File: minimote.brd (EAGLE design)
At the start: 160 x 100 mm, 41 parts, among them IC1 ATTINY441/841-SSU, J1 AVR_SPI_PROG_3X2PTH, T1 2N3904

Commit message: moved parts around
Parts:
- removed U$3: EDGEUSB, minimote:USBPCB
- added U$13: EDGEUSB, minimote:USBPCB
- moved R10 141.0 mm to (3.81, 38.1), turned to 270 degrees
- moved R9 137.4 mm to (7.62, 38.1), turned to 270 degrees
- moved R8 134.9 mm to (11.4, 38.1), turned to 90 degrees
- moved C1 132.1 mm to (7.62, 29.2), turned to 90 degrees
- moved U$2 130.3 mm to (15.2, 38.1)
- moved C2 129.6 mm to (10.2, 29.2), turned to 90 degrees
- moved U$1 127.3 mm to (20.3, 38.1)
- moved R12 123.4 mm to (3.81, 30.5)
- moved R11 122.6 mm to (3.81, 27.9)
- moved R13 122.5 mm to (3.81, 19.1), turned to 270 degrees
- moved RN1 108.1 mm to (43.2, 63.5), turned to 90 degrees
- moved R1 100.1 mm to (17.8, 19.1), turned to 270 degrees
- moved R6 86.4 mm to (14.0, 19.1), turned to 270 degrees
- moved D2 83.7 mm to (25.4, 38.1)
- moved R4 83.0 mm to (25.4, 19.1), turned to 270 degrees
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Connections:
- new net N$123: D4.C, D5.A, D6.A, R1.2
- new net N$124: D1.C, D3.A, D4.A, D5.C, R4.2
- new net N$125: D1.A, D3.C, D6.C, R7.2
- net GND: now also U$13.GND; no longer U$3.GND
- net LED1: no longer D1.A, D3.C, D6.C, R7.2
- net LED2: no longer D1.C, D3.A, D4.A, D5.C, R4.2
- net LED3: no longer D4.C, D5.A, D6.A, R1.2
- net N$8: now also U$13.DM; no longer U$3.DM
- net N$9: now also U$13.DP; no longer U$3.DP
- net V_USB: now also U$13.VCC; no longer U$3.VCC
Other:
- board size 160 x 100 mm -> 85.6 x 54.2 mm

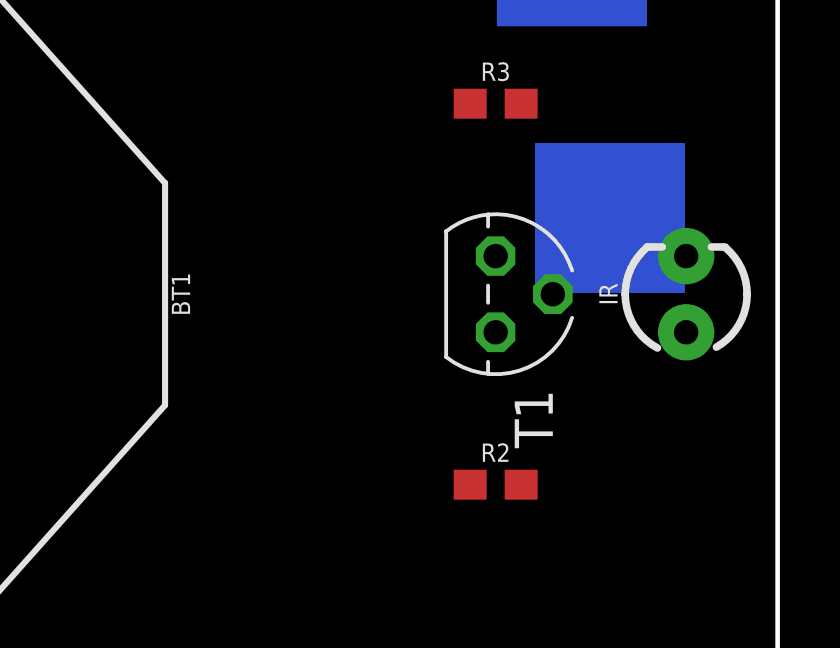
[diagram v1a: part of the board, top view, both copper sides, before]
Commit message: changed 3904 to smt component
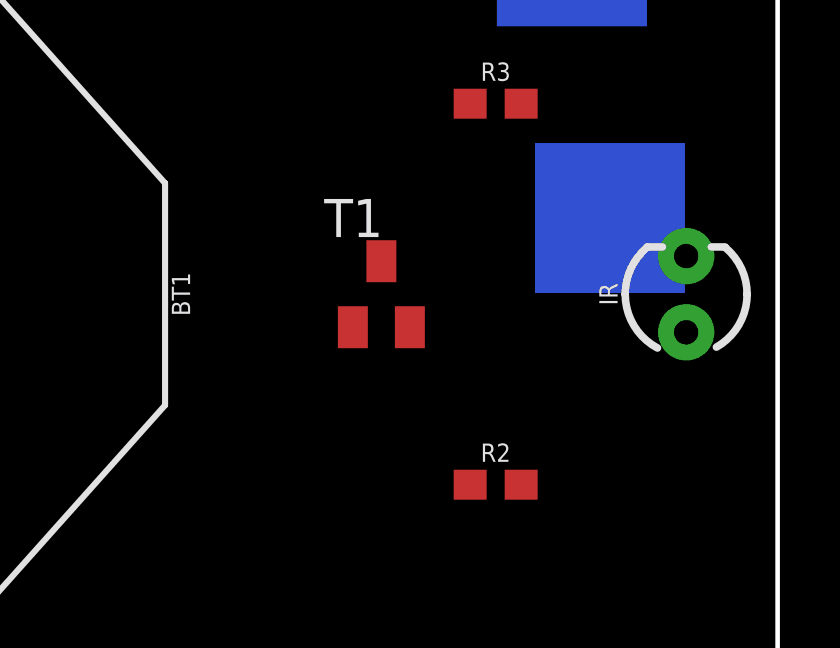
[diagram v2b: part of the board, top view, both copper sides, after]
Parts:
- T1: value 2N3904 -> (none); device transistor:TO92 -> transistor:SOT23-BEC
- moved T1 3.81 mm to (72.4, 27.9), turned to 0 degrees
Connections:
- net GND: now also T1.E; no longer T1.3
- net N$2: now also T1.C; no longer T1.1
- net N$3: now also T1.B; no longer T1.2
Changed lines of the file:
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@@
 <attribute name="SF_SKU" value="COM-08720" x="69.85" y="41.91" size="1.778" layer="27" rot="R90" display="off"/>
 </element>
-<element name="T1" library="transistor" library_urn="urn:adsk.eagle:library:402" package="TO92" package3d_urn="urn:adsk.eagle:package:29893/2" value="2N3904" x="76.2" y="27.94" rot="R270"/>
 <element name="U$1" library="minimote" package="SOT23" value="SI2301" x="20.32" y="38.1"/>
 <element name="R8" library="SparkFun-Resistors" library_urn="urn:adsk.eagle:library:532" package="0603" package3d_urn="urn:adsk.eagle:package:39650/1" value="10k" x="11.43" y="38.1" rot="R90">
@@
 <element name="U$13" library="minimote" package="USBPCB" value="EDGEUSB" x="0" y="22.86" rot="R90"/>
 <element name="U$4" library="minimote" package="SOT23" value="AZ23C3V6" x="8.89" y="19.05" rot="R180"/>
+<element name="T1" library="transistor" library_urn="urn:adsk.eagle:library:402" package="SOT23-BEC" package3d_urn="urn:adsk.eagle:package:29919/2" value="" x="72.39" y="27.94"/>
 </elements>
 <signals>
@@
 <contactref element="BT1" pad="2"/>
 <contactref element="J1" pad="6"/>
-<contactref element="T1" pad="3"/>
 <contactref element="S2" pad="3"/>
 <contactref element="S2" pad="4"/>
@@
 <contactref element="U$13" pad="GND"/>
 <contactref element="U$4" pad="3"/>
-<wire x1="71.755" y1="44.704" x2="76.2" y2="29.21" width="0" layer="19" extent="1-1"/>
+<contactref element="T1" pad="E"/>
 <wire x1="71.755" y1="39.116" x2="71.755" y2="44.704" width="0" layer="19" extent="1-1"/>
-<wire x1="54.61" y1="27.94" x2="71.755" y2="44.704" width="0" layer="19" extent="1-1"/>
+<wire x1="54.61" y1="27.94" x2="71.755" y2="39.116" width="0" layer="19" extent="1-1"/>
 <wire x1="35.56" y1="26.67" x2="54.61" y2="27.94" width="0" layer="19" extent="1-1"/>
-<wire x1="10.16" y1="30.06" x2="35.56" y2="26.67" width="0" layer="19" extent="1-1"/>
+<wire x1="16.19" y1="37" x2="35.56" y2="26.67" width="0" layer="19" extent="1-1"/>
+<wire x1="13.97" y1="32.21" x2="16.19" y2="37" width="0" layer="19" extent="1-1"/>
+<wire x1="10.16" y1="30.06" x2="13.97" y2="32.21" width="0" layer="19" extent="1-1"/>
 <wire x1="7.62" y1="30.06" x2="10.16" y2="30.06" width="0" layer="19" extent="1-1"/>
-<wire x1="16.19" y1="37" x2="7.62" y2="30.06" width="0" layer="19" extent="1-1"/>
-<wire x1="13.97" y1="32.21" x2="16.19" y2="37" width="0" layer="19" extent="1-1"/>
-<wire x1="-6.35" y1="32.7025" x2="13.97" y2="32.21" width="0" layer="19" extent="1-1"/>
-<wire x1="8.89" y1="17.95" x2="-6.35" y2="32.7025" width="0" layer="19" extent="1-1"/>
+<wire x1="8.89" y1="17.95" x2="10.16" y2="30.06" width="0" layer="19" extent="1-1"/>
+<wire x1="-6.35" y1="32.7025" x2="7.62" y2="30.06" width="0" layer="19" extent="1-1"/>
+<wire x1="73.34" y1="26.84" x2="8.89" y2="17.95" width="0" layer="19" extent="1-1"/>
 </signal>
 <signal name="VCC">
@@
 </signal>
 <signal name="N$2">
-<contactref element="T1" pad="1"/>
 <contactref element="IR" pad="K"/>
-<wire x1="82.55" y1="29.21" x2="76.2" y2="26.67" width="0" layer="19" extent="1-1"/>
-</signal>
-<signal name="N$3">
-<contactref element="T1" pad="2"/>
-<contactref element="R3" pad="2"/>
-<wire x1="77.05" y1="34.29" x2="78.105" y2="27.94" width="0" layer="19" extent="1-1"/>
+<contactref element="T1" pad="C"/>
+<wire x1="72.39" y1="29.04" x2="82.55" y2="29.21" width="0" layer="19" extent="1-1"/>
 </signal>
 <signal name="N$1">
@@
 <wire x1="70.243" y1="48.26" x2="77.863" y2="59.69" width="0" layer="19" extent="16-16"/>
 </signal>
+<signal name="N$3">
+<contactref element="R3" pad="2"/>
+<contactref element="T1" pad="B"/>
+<wire x1="71.44" y1="26.84" x2="77.05" y2="34.29" width="0" layer="19" extent="1-1"/>
+</signal>
 </signals>
